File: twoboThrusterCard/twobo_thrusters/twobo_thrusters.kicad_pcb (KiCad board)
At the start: 2 copper layers, 86.2 x 52.5 mm, 13 parts, among them J2 Conn_01x09

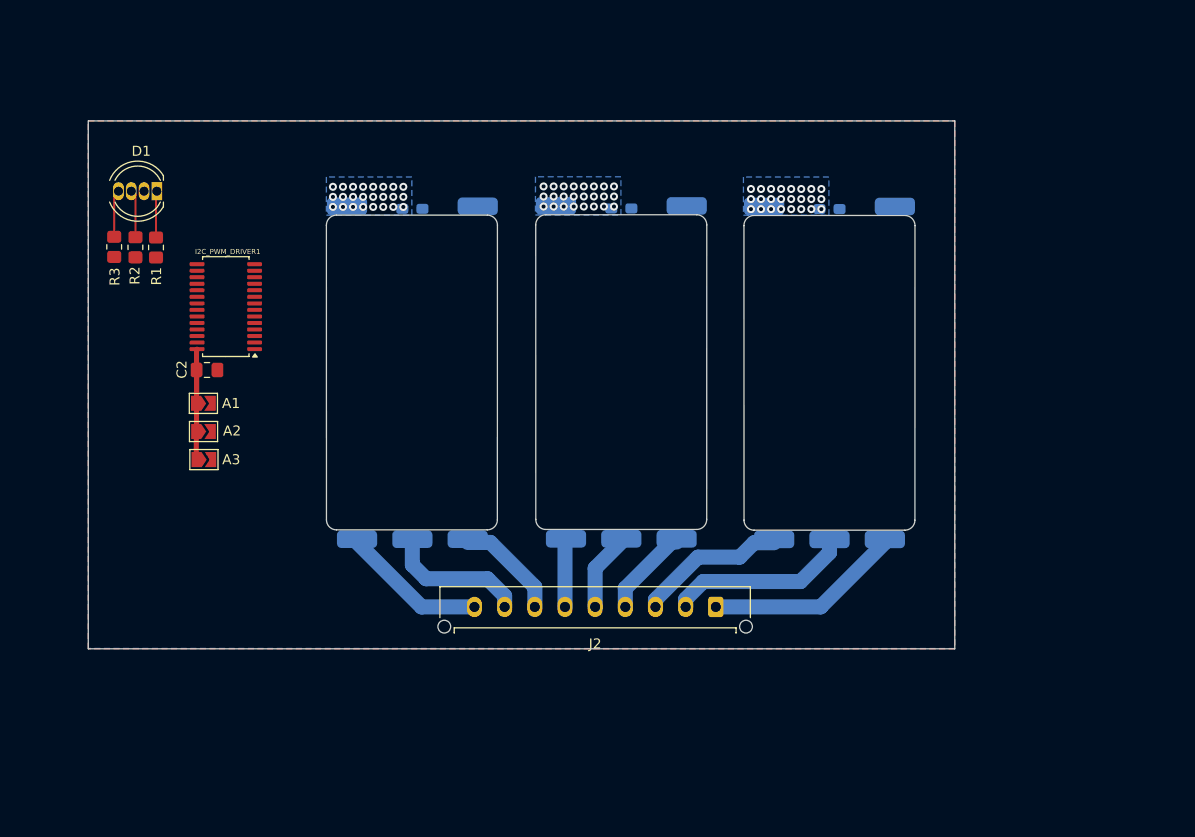
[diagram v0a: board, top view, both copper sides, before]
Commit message: Thruster card
added the stack up connector.
first iteration of routing
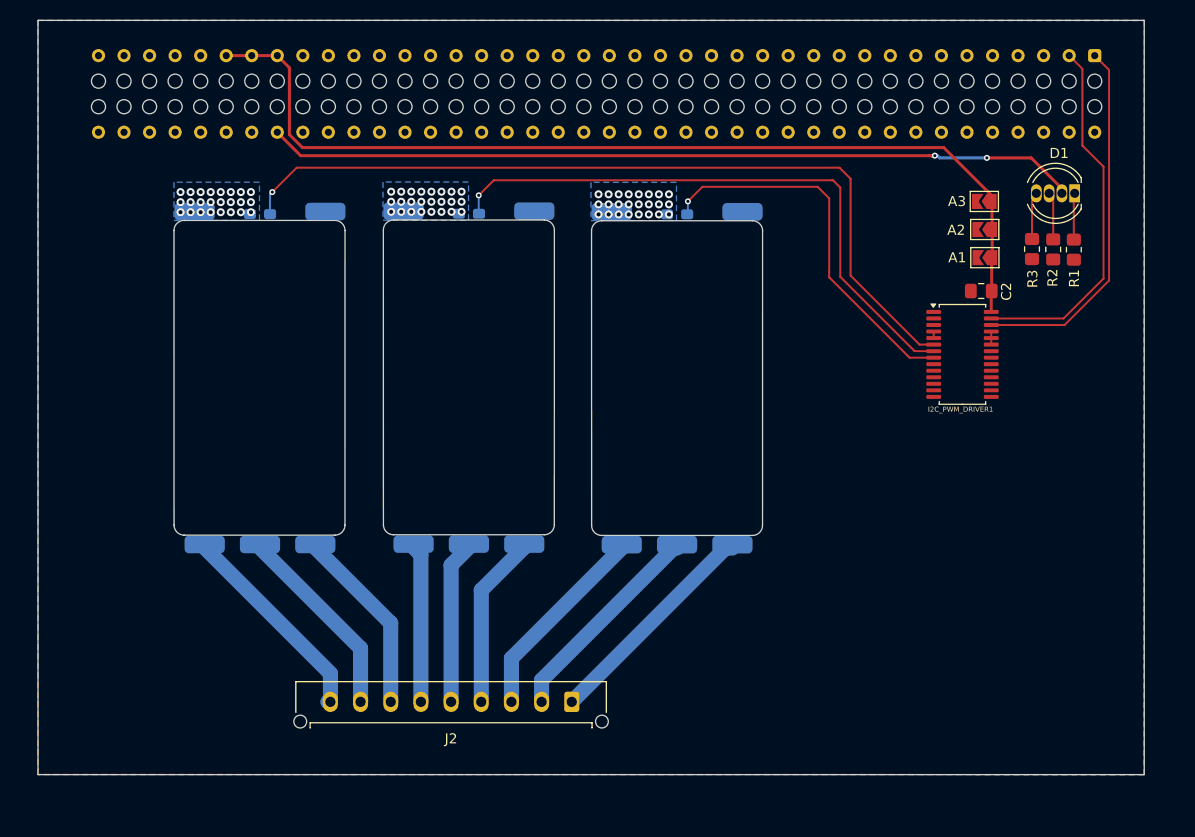
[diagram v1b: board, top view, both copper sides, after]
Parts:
- added J5: Conn_02x40_Odd_Even, custom_components:Samtec_HLE-140-02-L-DV-PE_2x40_P2.54mm_Horizontal, B.Cu at (155.1, 53.5)
- moved D1 91.3 mm to (153.1, 67.2)
- moved R1 91.3 mm to (153.0, 72.8)
- moved R3 91.3 mm to (148.8, 72.7)
- moved R2 91.3 mm to (150.9, 72.8)
- moved A3 81.7 mm to (144.1, 68.0), turned to 180 degrees
- moved A2 80.2 mm to (144.1, 70.8), turned to 180 degrees
- moved A1 79.0 mm to (144.2, 73.6), turned to 180 degrees
- moved C2 77.4 mm to (143.8, 76.9), turned to 180 degrees
- moved I2C_PWM_DRIVER1 73.4 mm to (141.9, 83.2), turned to 0 degrees
- moved J2 17.2 mm to (103.1, 117.8)
- moved U2 15.2 mm to (113.6, 85.6)
- moved U4 15.2 mm to (72.1, 85.6)
- moved U3 15.2 mm to (92.8, 85.5)
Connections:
- A1 pad 1: +5V -> +3.3V
- A2 pad 1: +5V -> +3.3V
- A3 pad 1: +5V -> +3.3V
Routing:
- net +3.3V: track 0.00 -> 97.4 mm
- net /PWM1: track 0.00 -> 82.0 mm, vias 0 -> 1
- net +5V: track 14.4 -> 80.9 mm, vias 0 -> 2
- net /PWM2: track 0.00 -> 60.0 mm, vias 0 -> 1
- net /PWM3: track 0.00 -> 38.0 mm, vias 0 -> 1
- net SCL: track 0.00 -> 36.5 mm
- net SDA: track 0.00 -> 36.4 mm
- net /C2: track 6.49 -> 15.7 mm
- net /A2: track 8.86 -> 17.6 mm
- net /B2: track 7.53 -> 16.1 mm
- net /A3: track 10.5 -> 18.4 mm
- net /C3: track 14.3 -> 20.8 mm
- net /B3: track 13.8 -> 19.5 mm
- net /C1: track 14.9 -> 19.8 mm
- net /B1: track 18.0 -> 21.1 mm
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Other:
- board size 86.2 x 52.5 mm -> 110 x 75 mm

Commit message: Repositioned Thruster Board Connector
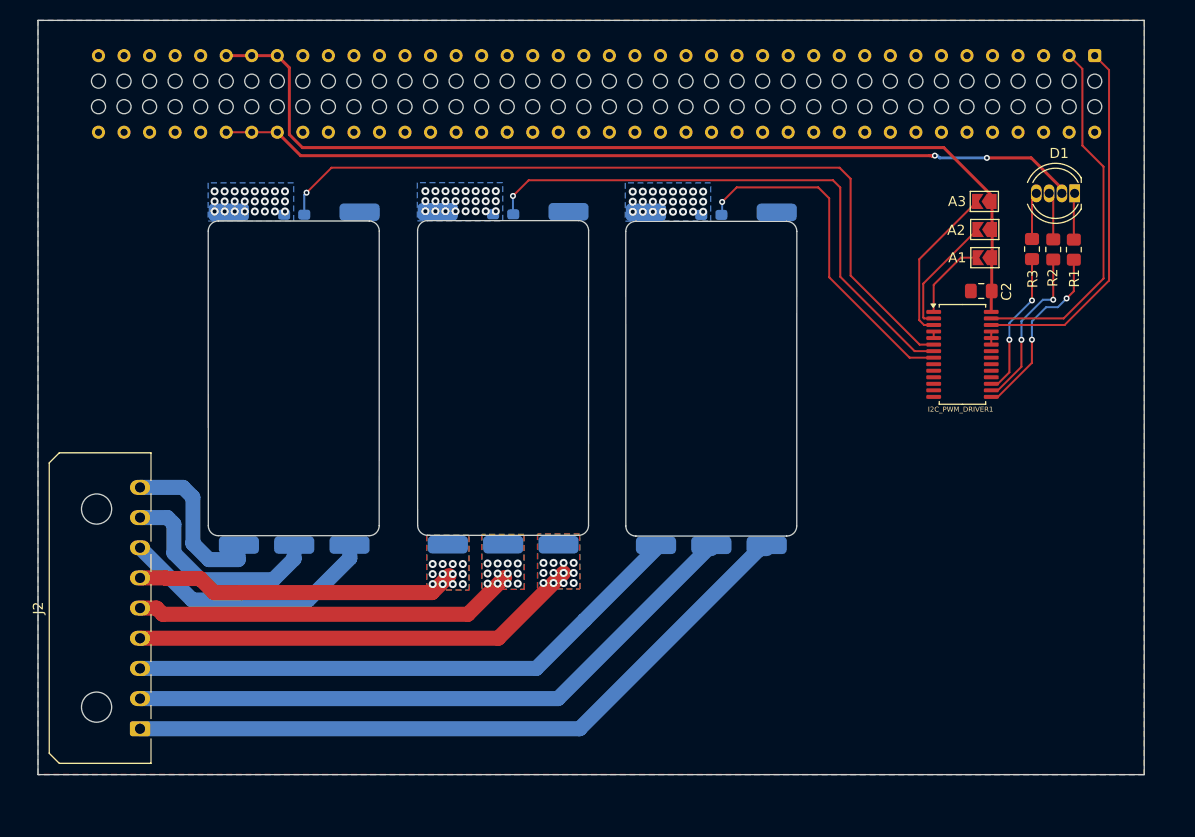
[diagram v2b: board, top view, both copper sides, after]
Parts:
- J2: footprint Connector_Molex:Molex_Micro-Fit_3.0_43650-0915_1x09_P3.00mm_Vertical -> Connector_Molex:Molex_Micro-Fit_3.0_43650-0900_1x09_P3.00mm_Horizontal
- moved J2 43.0 mm to (60.1, 120.4), turned to 90 degrees
- moved U2 3.40 mm to (117.0, 85.6)
- moved U3 3.40 mm to (96.3, 85.6)
- moved U4 3.40 mm to (75.5, 85.6)
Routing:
- net /A1: track 22.3 -> 69.7 mm
- net /B1: track 21.1 -> 63.0 mm
- net /C1: track 19.8 -> 56.2 mm
- net /A2: track 17.6 -> 44.8 mm, vias 0 -> 12
- net /B2: track 16.1 -> 38.0 mm, vias 0 -> 12
- net Net-(I2C_PWM_DRIVER1-PWM8): track 0.00 -> 18.1 mm, vias 0 -> 2
- net Net-(I2C_PWM_DRIVER1-PWM9): track 0.00 -> 16.6 mm, vias 0 -> 2
- net /C2: track 15.7 -> 32.0 mm, vias 0 -> 12
- net Net-(A3-B): track 0.00 -> 15.8 mm
- net Net-(I2C_PWM_DRIVER1-PWM10): track 0.00 -> 14.5 mm, vias 0 -> 2
- net Net-(A2-B): track 0.00 -> 12.1 mm
- net Net-(A1-B): track 0.00 -> 8.18 mm
- net /A3: track 18.4 -> 25.1 mm
- net +5V: track 80.9 -> 85.9 mm
- net /C3: track 20.8 -> 15.8 mm
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- added copper zone on B.Cu, net /A2
- added copper zone on F.Cu, net /A2
- added copper zone on B.Cu, net /B2
- added copper zone on F.Cu, net /B2
- added copper zone on B.Cu, net /C2
- added copper zone on F.Cu, net /C2
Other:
- outline, holes or cut-outs redrawn

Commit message: Added Silkscreen
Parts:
- added G***: LOGO, LOGO, F.Cu at (84.6, 118.4)
- added G***: LOGO, LOGO, B.Cu at (141.6, 102.4)
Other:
- board text added: "2026"
- board text added: "Twobo Thruster Card"

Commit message: Viewed Files
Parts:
- added H1: MountingHole, MountingHole:MountingHole_2.2mm_M2, F.Cu at (155.0, 85.0)
- added H2: MountingHole, MountingHole:MountingHole_2.2mm_M2, F.Cu at (55.0, 70.0)
- added H3: MountingHole, MountingHole:MountingHole_2.2mm_M2, F.Cu at (155.0, 120.0)
- added H4: MountingHole, MountingHole:MountingHole_2.2mm_M2, F.Cu at (55.0, 85.0)

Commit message: Repositioned Mounting Holes
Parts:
- removed H4: MountingHole, MountingHole:MountingHole_2.2mm_M2
- moved H1 32.4 mm to (160.0, 53.0)
- moved H2 17.5 mm to (51.0, 53.0)
- moved H3 5.35 mm to (160.0, 122.0)
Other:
- board size 110 x 75 mm -> 114.6 x 75 mm
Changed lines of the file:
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@@
 	(footprint "MountingHole:MountingHole_2.2mm_M2"
 		(layer "F.Cu")
-		(at 155.01 85.013495)
+		(at 159.985 52.975)
 		(descr "Mounting Hole 2.2mm, M2, no annular, generated by kicad-footprint-generator mountinghole.py")
 		(tags "mountinghole M2")
 		(property "Reference" "H1"
-			(at 0 -3.15 0)
+			(at -0.219 3.413 0)
 			(layer "F.SilkS")
 			(effects
@@
 	(footprint "MountingHole:MountingHole_2.2mm_M2"
 		(layer "F.Cu")
-		(at 155.01 120.013495)
+		(at 159.985 121.975)
 		(descr "Mounting Hole 2.2mm, M2, no annular, generated by kicad-footprint-generator mountinghole.py")
 		(tags "mountinghole M2")
@@
 	(footprint "MountingHole:MountingHole_2.2mm_M2"
 		(layer "F.Cu")
-		(at 55 85.00507)
-		(descr "Mounting Hole 2.2mm, M2, no annular, generated by kicad-footprint-generator mountinghole.py")
-		(tags "mountinghole M2")
-		(property "Reference" "H4"
-			(at 0 -3.15 0)
-			(layer "F.SilkS")
-			(effects
-				(font
-					(size 1 1)
-					(thickness 0.15)
-				)
-			)
-		)
-		(property "Value" "MountingHole"
-			(at 0 3.15 0)
-			(layer "F.Fab")
-			(effects
-				(font
-					(size 1 1)
-					(thickness 0.15)
-				)
-			)
-		)
-		(property "Datasheet" "~"
-			(at 0 0 0)
-			(layer "F.Fab")
-			(hide yes)
-			(effects
-				(font
-					(size 1.27 1.27)
-					(thickness 0.15)
-				)
-			)
-		)
-		(property "Description" "Mounting Hole without connection"
-			(at 0 0 0)
-			(layer "F.Fab")
-			(hide yes)
-			(effects
-				(font
-					(size 1.27 1.27)
-					(thickness 0.15)
-				)
-			)
-		)
-		(property ki_fp_filters "MountingHole*")
-		(sheetname "/")
-		(sheetfile "twobo_thrusters.kicad_sch")
-		(attr exclude_from_pos_files exclude_from_bom)
-		(fp_circle
-			(center 0 0)
-			(end 2.2 0)
-			(stroke
-				(width 0.15)
-				(type solid)
-			)
-			(fill no)
-			(layer "Cmts.User")
-		)
-		(fp_circle
-			(center 0 0)
-			(end 2.45 0)
-			(stroke
-				(width 0.05)
-				(type solid)
-			)
-			(fill no)
-			(layer "F.CrtYd")
-		)
-		(fp_text user "${REFERENCE}"
-			(at 0 0 0)
-			(layer "F.Fab")
-			(effects
-				(font
-					(size 1 1)
-					(thickness 0.15)
-				)
-			)
-		)
-		(pad "" np_thru_hole circle
-			(at 0 0)
-			(size 2.2 2.2)
-			(drill 2.2)
-			(layers "*.Cu" "*.Mask")
-		)
-		(embedded_fonts no)
-	)
-	(footprint "MountingHole:MountingHole_2.2mm_M2"
-		(layer "F.Cu")
-		(at 55 70.00507)
+		(at 50.995 52.975)
 		(descr "Mounting Hole 2.2mm, M2, no annular, generated by kicad-footprint-generator mountinghole.py")
 		(tags "mountinghole M2")
 		(property "Reference" "H2"
-			(at 0 -3.15 0)
+			(at 0.059 3.921 0)
 			(layer "F.SilkS")
 			(effects
@@
 		(tags "connector Samtec HLE horizontal")
 		(property "Reference" "J5"
-			(at -2.72 0.48 0)
+			(at -2.659 -3.645 0)
 			(layer "B.SilkS")
 			(effects
@@
 	)
 	(gr_rect
-		(start 50 50)
-		(end 160 125)
+		(start 48.4 50)
+		(end 163 125)
 		(stroke
 			(width 0.05)
@@
 		(polygon
 			(pts
-				(xy 49.999858 49.999945) (xy 160.007689 49.999945) (xy 159.99301 124.993928) (xy 50.014537 124.98116)
+				(xy 48.221858 50.253945) (xy 163.007689 50.999945) (xy 162.99301 125) (xy 48.222 125.254)
 			)
 		)
@@
 		(polygon
 			(pts
-				(xy 49.983621 50.00507) (xy 160.01 50.017839) (xy 160.01 125.013495) (xy 49.998296 125.000727)
+				(xy 48.221621 50.51307) (xy 163.01 50.017839) (xy 163.01 125.013495) (xy 48.236296 125.508727)
 			)
 		)
